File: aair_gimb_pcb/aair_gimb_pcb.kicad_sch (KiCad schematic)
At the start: 12 parts, among them U1 STM32F405RGTx, X1 8MHz

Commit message: mac update
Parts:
- removed B0, NR: SW_Push, Button_Switch_SMD:SW_Push_1P1T_NO_CK_KMR2, symbol Switch:SW_Push
- removed C1, C2: 15p, CRF1:SMD-0603_c, symbol Device:C_Small
- removed C3, C4, C5, C6, C7, C8: 2.2u, symbol Device:C_Small
- removed U1: STM32F405RGTx, Package_QFP:LQFP-64_10x10mm_P0.5mm, symbol MCU_ST_STM32F4:STM32F405RGTx
- removed X1: 8MHz, CRF1:Crystal_5x3mm, symbol crf_1:CRYSTAL_GROUND_PIN
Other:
- added sheet Stm32f405 (Stm32f405.kicad_sch)

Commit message: macros
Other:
- added sheet drv8302 (drv8302.kicad_sch)
- sheet Stm32f405 ports: added L1, L2, L3; removed none
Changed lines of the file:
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@@
 	(generator_version "9.0")
 	(paper "A4")
+	(wire
+		(pts
+			(xy 124.46 87.63) (xy 144.78 87.63)
+		)
+		(stroke
+			(width 0)
+			(type default)
+		)
+	)
+	(wire
+		(pts
+			(xy 124.46 85.09) (xy 144.78 85.09)
+		)
+		(stroke
+			(width 0)
+			(type default)
+		)
+	)
+	(wire
+		(pts
+			(xy 124.46 82.55) (xy 144.78 82.55)
+		)
+		(stroke
+			(width 0)
+			(type default)
+		)
+	)
 	(sheet
-		(at 124.46 87.63)
+		(at 144.78 76.2)
+		(size 48.26 38.1)
+		(exclude_from_sim no)
+		(in_bom yes)
+		(on_board yes)
+		(dnp no)
+		(fields_autoplaced yes)
+		(stroke
+			(width 0.1524)
+			(type solid)
+		)
+		(fill
+			(color 0 0 0 0.0000)
+		)
+		(property "Sheetname" "drv8302"
+			(at 144.78 75.4884 0)
+			(effects
+				(font
+					(size 1.27 1.27)
+				)
+				(justify left bottom)
+			)
+		)
+		(property "Sheetfile" "drv8302.kicad_sch"
+			(at 144.78 114.8846 0)
+			(effects
+				(font
+					(size 1.27 1.27)
+				)
+				(justify left top)
+			)
+		)
+		(pin "L3" input
+			(at 144.78 87.63 180)
+			(effects
+				(font
+					(size 1.27 1.27)
+				)
+				(justify left)
+			)
+		)
+		(pin "L2" input
+			(at 144.78 85.09 180)
+			(effects
+				(font
+					(size 1.27 1.27)
+				)
+				(justify left)
+			)
+		)
+		(pin "L1" input
+			(at 144.78 82.55 180)
+			(effects
+				(font
+					(size 1.27 1.27)
+				)
+				(justify left)
+			)
+		)
+		(instances
+			(project "aair_gimb_pcb"
+				(path "/d04c5395-2e3c-40b8-8677-11fb81ced555"
+					(page "3")
+				)
+			)
+		)
+	)
+	(sheet
+		(at 88.9 77.47)
 		(size 35.56 38.1)
 		(exclude_from_sim no)
@@
 		)
 		(property "Sheetname" "Stm32f405"
-			(at 124.46 86.9184 0)
+			(at 88.9 76.7584 0)
 			(effects
 				(font
@@
 		)
 		(property "Sheetfile" "Stm32f405.kicad_sch"
-			(at 124.46 126.3146 0)
+			(at 88.9 116.1546 0)
 			(effects
 				(font
@@
 			)
 		)
+		(pin "L3" output
+			(at 124.46 87.63 0)
+			(effects
+				(font
+					(size 1.27 1.27)
+				)
+				(justify right)
+			)
+		)
+		(pin "L2" output
+			(at 124.46 85.09 0)
+			(effects
+				(font
+					(size 1.27 1.27)
+				)
+				(justify right)
+			)
+		)
+		(pin "L1" output
+			(at 124.46 82.55 0)
+			(effects
+				(font
+					(size 1.27 1.27)
+				)
+				(justify right)
+			)
+		)

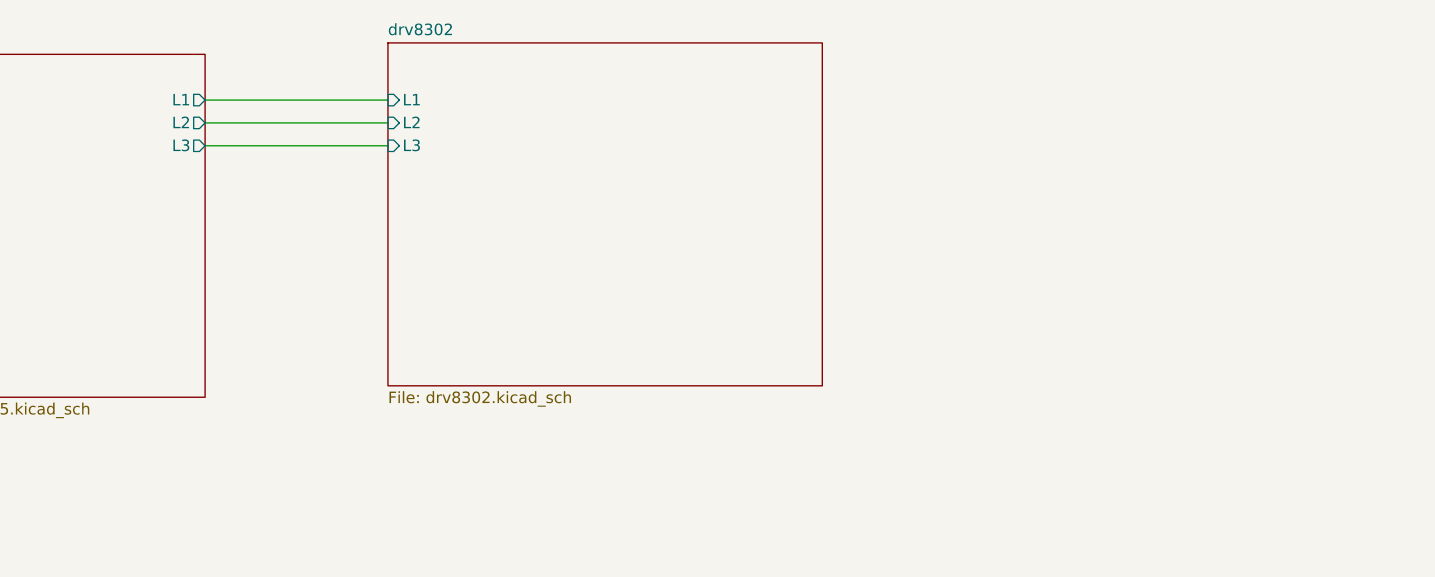
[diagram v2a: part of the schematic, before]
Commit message: add mosfet
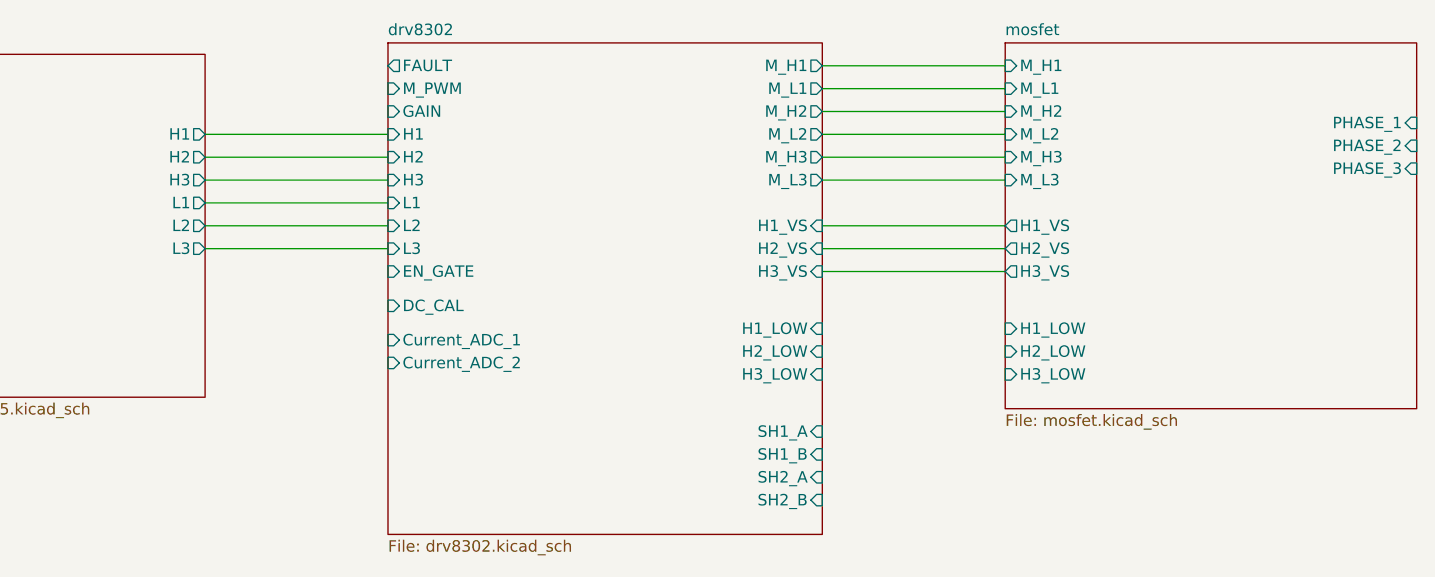
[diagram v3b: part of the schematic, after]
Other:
- added sheet mosfet (mosfet.kicad_sch)
- sheet Stm32f405 ports: added H1, H2, H3; removed none
- sheet drv8302 ports: added Current_ADC_1, Current_ADC_2, DC_CAL, EN_GATE, FAULT, GAIN, H1, H1_LOW, H1_VS, H2, H2_LOW, H2_VS, H3, H3_LOW, H3_VS, M_H1, M_H2, M_H3, M_L1, M_L2, M_L3, M_PWM, SH1_A, SH1_B, SH2_A, SH2_B; removed none

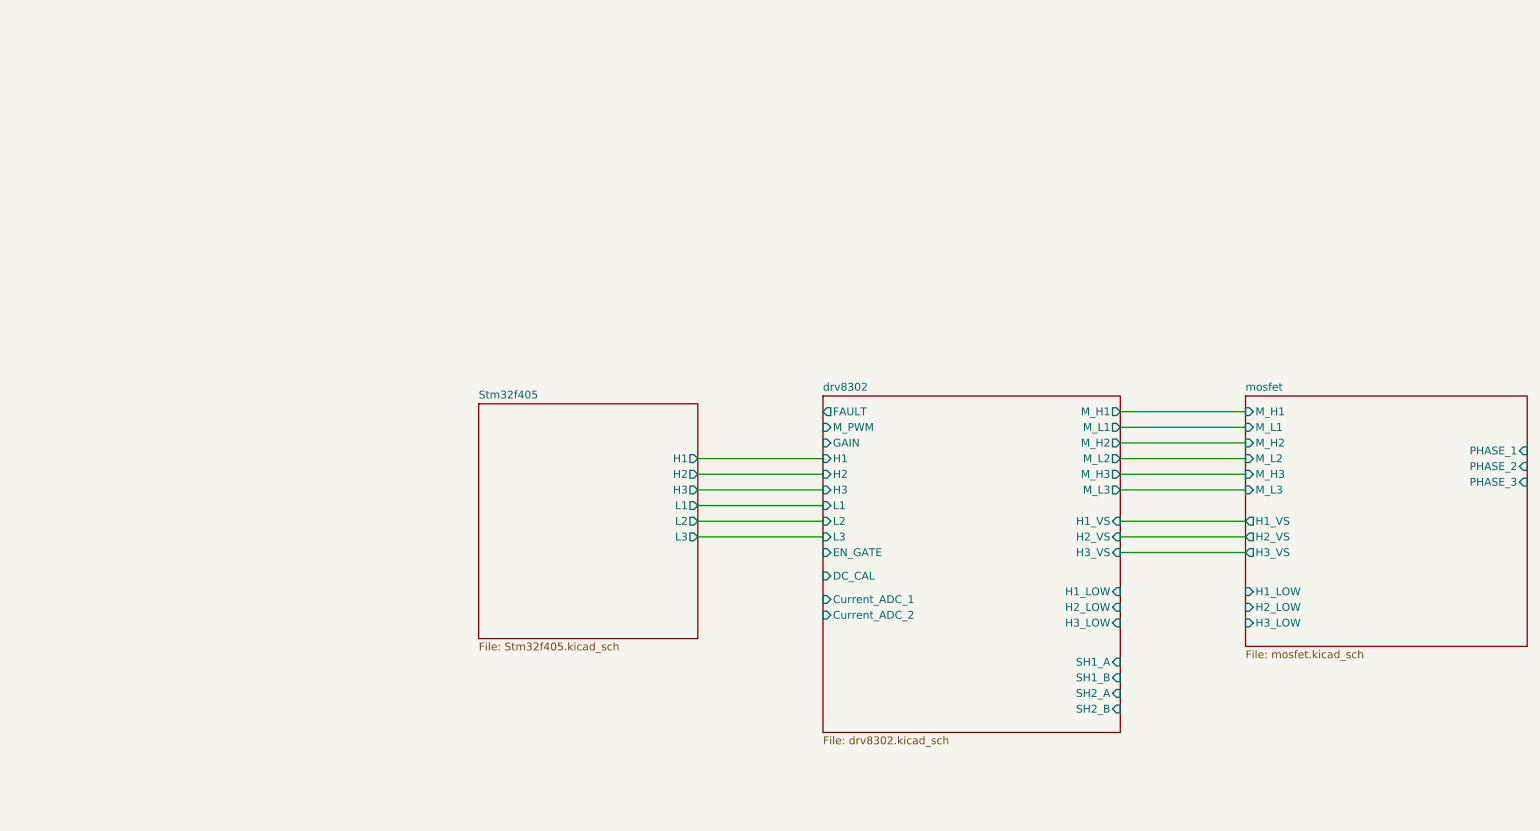
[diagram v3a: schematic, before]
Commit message: сделать коннектор для переыерии
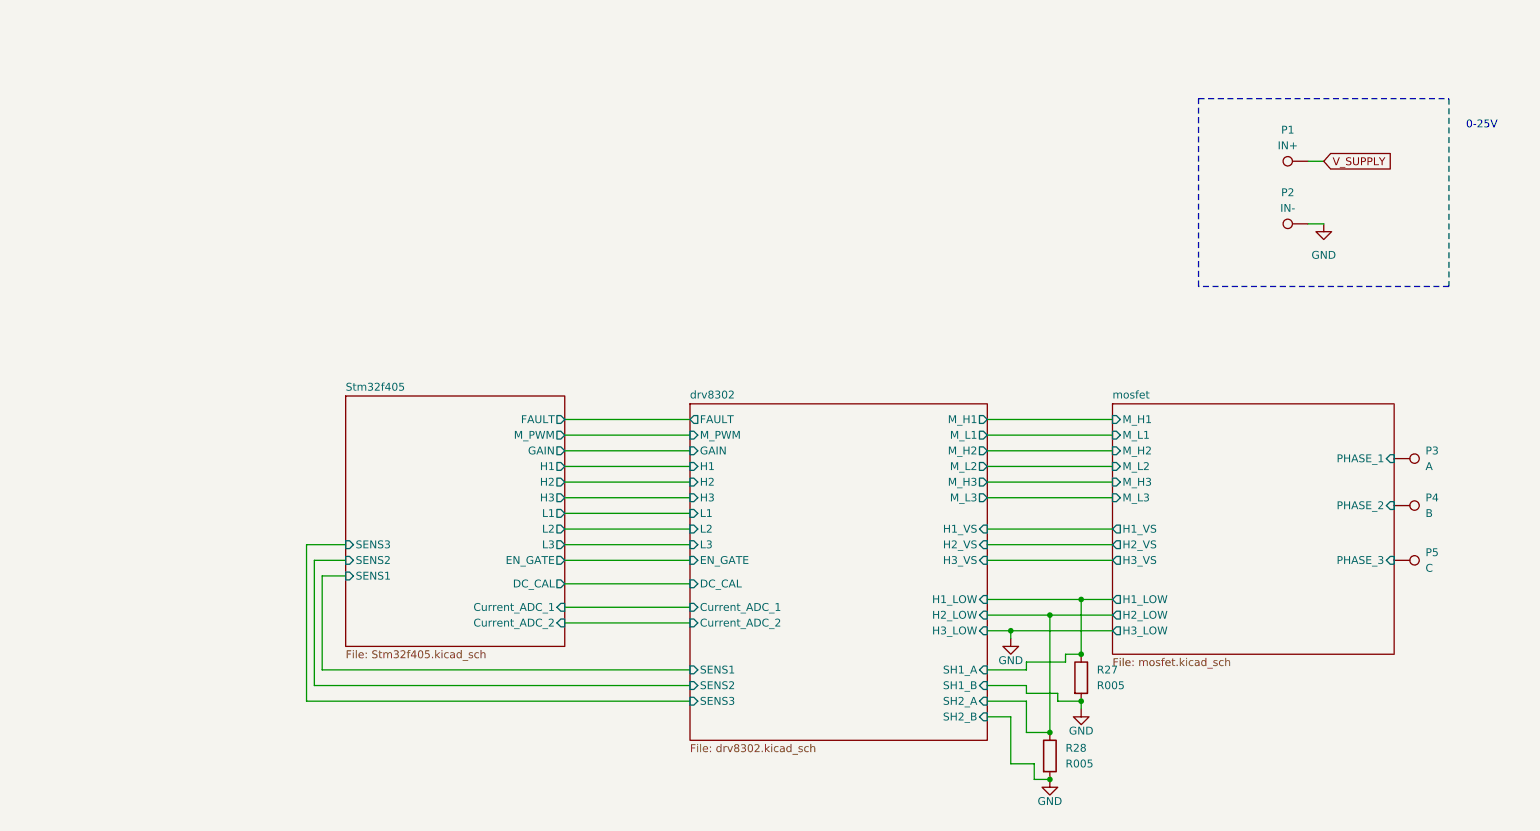
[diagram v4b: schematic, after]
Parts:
- added P1: IN+, CRF1:1PAD_4x5mm, symbol Connector:TestPoint
- added P2: IN-, CRF1:1PAD_4x5mm, symbol Connector:TestPoint
- added P3: A, CRF1:1PAD_4x5mm, symbol Connector:TestPoint
- added P4: B, CRF1:1PAD_4x5mm, symbol Connector:TestPoint
- added P5: C, CRF1:1PAD_4x5mm, symbol Connector:TestPoint
- added R27, R28: R005, Resistor_SMD:R_2512_6332Metric, symbol Device:R
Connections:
- net drv8302/H1_LOW: now also R27.1
- net drv8302/H2_LOW: now also R28.1
- net mosfet/PHASE_1: now also P3.1
- net mosfet/PHASE_2: now also P4.1
- net mosfet/PHASE_3: now also P5.1
- new net GND: P2.1, R27.2, R28.2
- new net V_SUPPLY: P1.1
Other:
- sheet Stm32f405 ports: added Current_ADC_1, Current_ADC_2, DC_CAL, EN_GATE, FAULT, GAIN, M_PWM, SENS1, SENS2, SENS3; removed none
- sheet drv8302 ports: added SENS1, SENS2, SENS3; removed none
- note added: "0-25V"

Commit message: pcb
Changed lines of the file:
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@@
 		(on_board yes)
 		(dnp no)
-		(fields_autoplaced yes)
 		(property "Reference" "P1"
-			(at 220.218 33.02 90)
+			(at 220.472 35.814 90)
 			(effects
 				(font
@@
 					(size 1.27 1.27)
 				)
+				(hide yes)
 			)
 		)
@@
 		(on_board yes)
 		(dnp no)
-		(fields_autoplaced yes)
 		(property "Reference" "P2"
-			(at 220.218 43.18 90)
+			(at 220.472 45.72 90)
 			(effects
 				(font
@@
 					(size 1.27 1.27)
 				)
+				(hide yes)
 			)
 		)

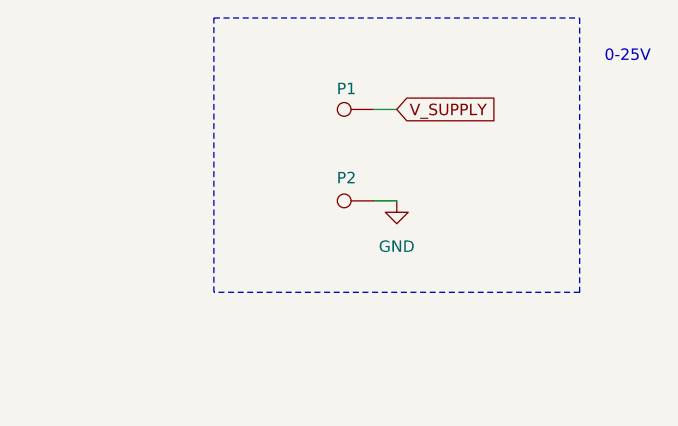
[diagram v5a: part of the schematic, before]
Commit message: add digital logic to pcb
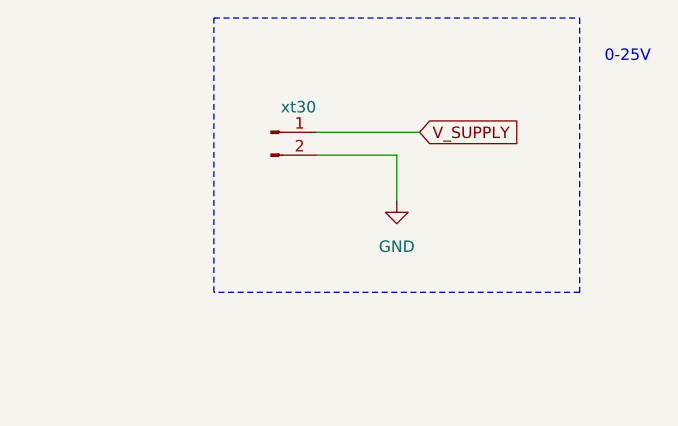
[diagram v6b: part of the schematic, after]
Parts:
- removed P1: IN+, CRF1:1PAD_4x5mm, symbol Connector:TestPoint
- removed P2: IN-, CRF1:1PAD_4x5mm, symbol Connector:TestPoint
- added xt30: XT30, Connector_AMASS:AMASS_XT30PW-M_1x02_P2.50mm_Horizontal, symbol Connector:Conn_01x02_Pin
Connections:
- net GND: now also xt30.2 (Pin_2)
- net V_SUPPLY: now also xt30.1 (Pin_1)
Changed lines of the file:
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@@
+	(wire
+		(pts
+			(xy 217.17 43.18) (xy 226.06 43.18)
+		)
+		(stroke
+			(width 0)
+			(type default)
+		)
+	)
 	(wire
 		(pts
@@
 	(wire
 		(pts
-			(xy 223.52 38.1) (xy 226.06 38.1)
-		)
-		(stroke
-			(width 0)
-			(type default)
-		)
-	)
-	(wire
-		(pts
 			(xy 182.88 124.46) (xy 182.88 125.73)
 		)
@@
 	(wire
 		(pts
+			(xy 217.17 40.64) (xy 228.6 40.64)
+		)
+		(stroke
+			(width 0)
+			(type default)
+		)
+	)
+	(wire
+		(pts
 			(xy 171.45 92.71) (xy 191.77 92.71)
 		)
@@
 	(wire
 		(pts
+			(xy 226.06 43.18) (xy 226.06 48.26)
+		)
+		(stroke
+			(width 0)
+			(type default)
+		)
+	)
+	(wire
+		(pts
 			(xy 62.23 102.87) (xy 67.31 102.87)
 		)
@@
 		(pts
 			(xy 177.8 119.38) (xy 177.8 120.65)
-		)
-		(stroke
-			(width 0)
-			(type default)
-		)
-	)
-	(wire
-		(pts
-			(xy 223.52 48.26) (xy 226.06 48.26)
 		)
 		(stroke
@@
 	(global_label "V_SUPPLY"
 		(shape input)
-		(at 226.06 38.1 0)
+		(at 228.6 40.64 0)
 		(fields_autoplaced yes)
 		(effects
@@
 		)
 		(property "Intersheetrefs" "${INTERSHEET_REFS}"
-			(at 238.2981 38.1 0)
+			(at 240.8381 40.64 0)
 			(effects
 				(font
@@
 	)
 	(symbol
-		(lib_id "Connector:TestPoint")
-		(at 223.52 38.1 90)
+		(lib_id "Connector:Conn_01x02_Pin")
+		(at 212.09 40.64 0)
 		(unit 1)
 		(exclude_from_sim no)
@@
 		(on_board yes)
 		(dnp no)
-		(property "Reference" "P1"
-			(at 220.472 35.814 90)
-			(effects
-				(font
-					(size 1.27 1.27)
-				)
-			)
-		)
-		(property "Value" "IN+"
-			(at 220.218 35.56 90)
-			(effects
-				(font
-					(size 1.27 1.27)
-				)
-				(hide yes)
-			)
-		)
-		(property "Footprint" "CRF1:1PAD_4x5mm"
-			(at 223.52 33.02 0)
+		(property "Reference" "xt30"
+			(at 215.138 37.846 0)
+			(effects
+				(font
+					(size 1.27 1.27)
+				)
+			)
+		)
+		(property "Value" "XT30"
+			(at 212.725 38.1 0)
+			(effects
+				(font
+					(size 1.27 1.27)
+				)
+				(hide yes)
+			)
+		)
+		(property "Footprint" "Connector_AMASS:AMASS_XT30PW-M_1x02_P2.50mm_Horizontal"
+			(at 212.09 40.64 0)
 			(effects
 				(font
@@
 		)
 		(property "Datasheet" "~"
-			(at 223.52 33.02 0)
-			(effects
-				(font
-					(size 1.27 1.27)
-				)
-				(hide yes)
-			)
-		)
-		(property "Description" "test point"
-			(at 223.52 38.1 0)
+			(at 212.09 40.64 0)
+			(effects
+				(font
+					(size 1.27 1.27)
+				)
+				(hide yes)
+			)
+		)
+		(property "Description" "Generic connector, single row, 01x02, script generated"
+			(at 212.09 40.64 0)
 			(effects
 				(font
@@
 		)
 		(pin "1"
+		)
+		(pin "2"
 		)
 		(instances
 			(project ""
 				(path "/d04c5395-2e3c-40b8-8677-11fb81ced555"
-					(reference "P1")
+					(reference "xt30")
 					(unit 1)
 				)
-			)
-		)
-	)
-	(symbol
-		(lib_id "Connector:TestPoint")
-		(at 223.52 48.26 90)
-		(unit 1)
-		(exclude_from_sim no)
-		(in_bom yes)
-		(on_board yes)
-		(dnp no)
-		(property "Reference" "P2"
-			(at 220.472 45.72 90)
-			(effects
-				(font
-					(size 1.27 1.27)
-				)
-			)
-		)
-		(property "Value" "IN-"
-			(at 220.218 45.72 90)
-			(effects
-				(font
-					(size 1.27 1.27)
-				)
-				(hide yes)
-			)
-		)
-		(property "Footprint" "CRF1:1PAD_4x5mm"
-			(at 223.52 43.18 0)
-			(effects
-				(font
-					(size 1.27 1.27)
-				)
-				(hide yes)
-			)
-		)
-		(property "Datasheet" "~"
-			(at 223.52 43.18 0)
-			(effects
-				(font
-					(size 1.27 1.27)
-				)
-				(hide yes)
-			)
-		)
-		(property "Description" "test point"
-			(at 223.52 48.26 0)
-			(effects
-				(font
-					(size 1.27 1.27)
-				)
-				(hide yes)
-			)
-		)
-		(pin "1"
-		)
-		(instances
-			(project "aair_gimb_pcb"
-				(path "/d04c5395-2e3c-40b8-8677-11fb81ced555"
-					(reference "P2")
-					(unit 1)
-				)
